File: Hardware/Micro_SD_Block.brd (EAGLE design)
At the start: 30.5 x 44.5 mm, 16 parts, among them U1 USD-SOCKETNEW, U2 EDISON_CONNECTOR_FULLMOUNTING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, U3 EDISON_CONNECTOR_FULLHEADER

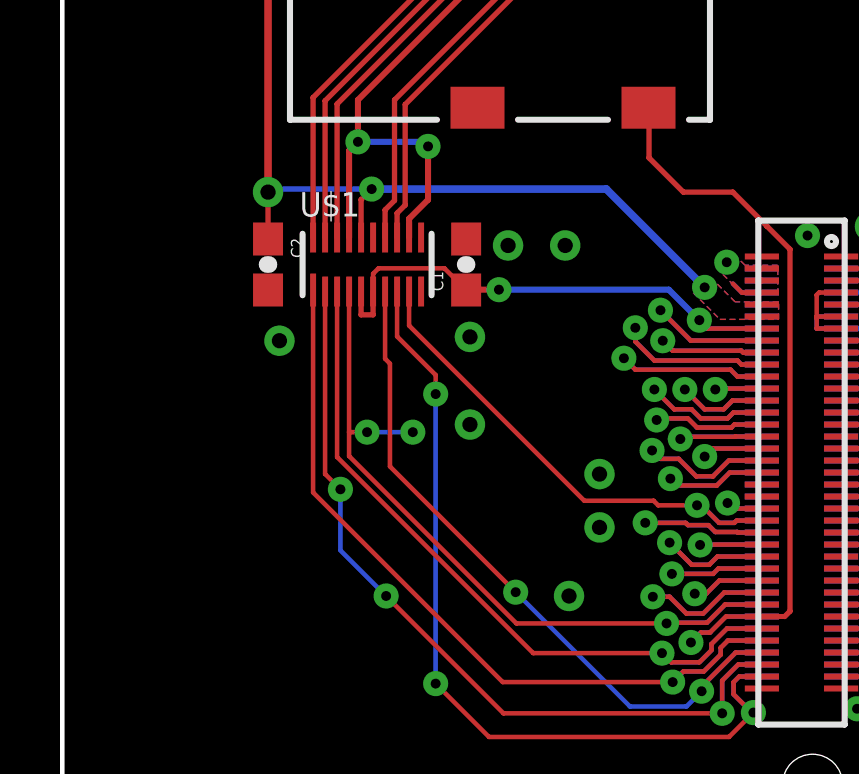
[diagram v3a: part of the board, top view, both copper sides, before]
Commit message: Ready for reds Struck one weird leftover via Renamed TXB0108 chip refdes To-do: fix the TXB0108 symbol to remove P$ from pin names. Do in library and update to design!
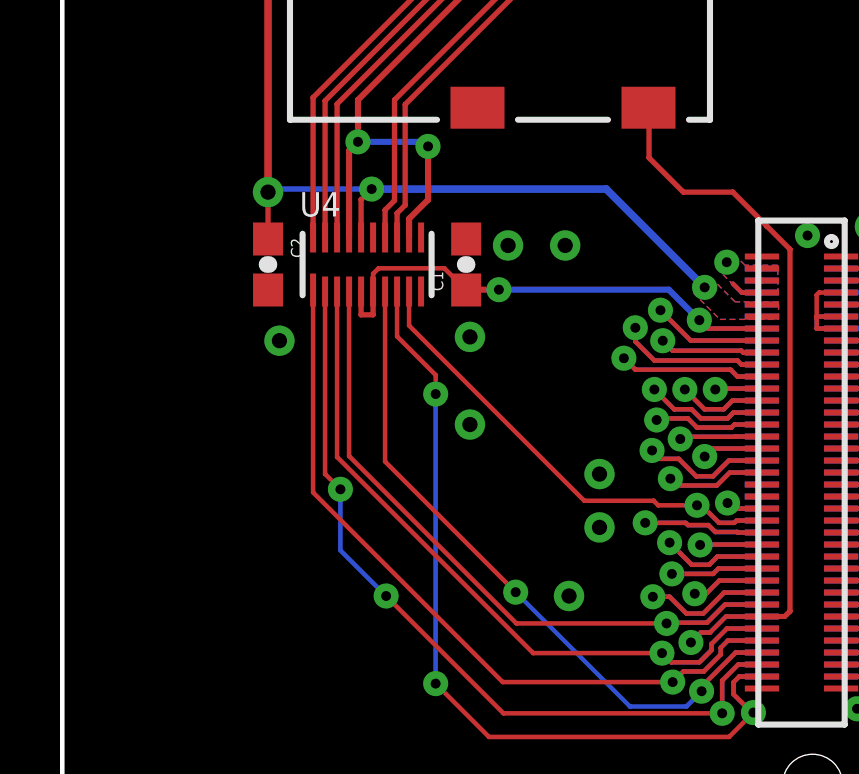
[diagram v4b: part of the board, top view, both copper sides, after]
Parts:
- renumbered U$1 to U4
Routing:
- net GP78_SD_0_CLK: track 27.4 -> 25.3 mm, vias 3 -> 1
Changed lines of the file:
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@@
 <setting verticaltext="up"/>
 </settings>
-<grid distance="0.005" unitdist="inch" unit="inch" style="lines" multiple="1" display="yes" altdistance="0.005" altunitdist="inch" altunit="inch"/>
+<grid distance="0.05" unitdist="inch" unit="inch" style="lines" multiple="1" display="yes" altdistance="0.005" altunitdist="inch" altunit="inch"/>
 <layers>
 <layer number="1" name="Top" color="4" fill="1" visible="yes" active="yes"/>
@@
 <layer number="21" name="tPlace" color="16" fill="1" visible="yes" active="yes"/>
 <layer number="22" name="bPlace" color="14" fill="1" visible="yes" active="yes"/>
-<layer number="23" name="tOrigins" color="15" fill="1" visible="no" active="yes"/>
-<layer number="24" name="bOrigins" color="15" fill="1" visible="no" active="yes"/>
+<layer number="23" name="tOrigins" color="15" fill="1" visible="yes" active="yes"/>
+<layer number="24" name="bOrigins" color="15" fill="1" visible="yes" active="yes"/>
 <layer number="25" name="tNames" color="7" fill="1" visible="no" active="yes"/>
 <layer number="26" name="bNames" color="7" fill="1" visible="no" active="yes"/>
@@
 <layer number="43" name="vRestrict" color="2" fill="10" visible="no" active="yes"/>
 <layer number="44" name="Drills" color="7" fill="1" visible="no" active="yes"/>
-<layer number="45" name="Holes" color="7" fill="1" visible="no" active="yes"/>
+<layer number="45" name="Holes" color="7" fill="1" visible="yes" active="yes"/>
 <layer number="46" name="Milling" color="3" fill="1" visible="no" active="yes"/>
-<layer number="51" name="tDocu" color="6" fill="1" visible="no" active="yes"/>
+<layer number="51" name="tDocu" color="6" fill="1" visible="yes" active="yes"/>
 <layer number="3" name="Route3" color="4" fill="3" visible="no" active="no"/>
 <layer number="4" name="Route4" color="1" fill="4" visible="no" active="no"/>
@@
 <layer number="251" name="SMDround" color="12" fill="11" visible="no" active="no"/>
 <layer number="254" name="cooling" color="7" fill="1" visible="no" active="no"/>
-<layer number="255" name="routoute" color="7" fill="1" visible="no" active="yes"/>
+<layer number="255" name="routoute" color="7" fill="1" visible="no" active="no"/>
 </layers>
 <board>
@@
 <element name="FID3" library="SparkFun-Aesthetics" package="FIDUCIAL-1X2" value="FIDUCIAL1X2" x="1.27" y="5.08" rot="MR0"/>
 <element name="FID4" library="SparkFun-Aesthetics" package="FIDUCIAL-1X2" value="FIDUCIAL1X2" x="25.4" y="43.18" rot="MR0"/>
-<element name="U$1" library="Testing" package="UFDFN-20" value="TXB0108" x="10.16" y="23.114"/>
+<element name="U4" library="Testing" package="UFDFN-20" value="TXB0108" x="10.16" y="23.114"/>
 <element name="C1" library="SparkFun-Capacitors" package="0603-CAP" value="0.1uF" x="13.462" y="23.114" rot="R90">
 <attribute name="PROD_ID" value="CAP-00810" x="13.462" y="23.114" size="1.778" layer="27" rot="R90" display="off"/>
@@
 <contactref element="U1" pad="CD2"/>
 <contactref element="U1" pad="GND1"/>
-<contactref element="U$1" pad="P$15"/>
+<contactref element="U4" pad="P$15"/>
 <contactref element="U1" pad="6"/>
 <contactref element="C1" pad="2"/>
@@
 <contactref element="U3" pad="8"/>
 <contactref element="U3" pad="10"/>
-<contactref element="U$1" pad="P$16"/>
+<contactref element="U4" pad="P$16"/>
 <contactref element="U1" pad="4"/>
 <via x="10.3124" y="25.6286" extent="1-16" drill="0.3302"/>
@@
 <wire x1="19.7104" y1="15.24" x2="19.8628" y2="15.0876" width="0.1524" layer="1"/>
 <wire x1="19.8628" y1="15.0876" x2="21.1582" y2="15.0876" width="0.1524" layer="1"/>
-<contactref element="U$1" pad="P$9"/>
+<contactref element="U4" pad="P$9"/>
 <wire x1="11.56" y1="22.214" x2="11.56" y2="21.079" width="0.1524" layer="1"/>
 <wire x1="11.56" y1="21.079" x2="17.399" y2="15.24" width="0.1524" layer="1"/>
@@
 <contactref element="U2" pad="58"/>
 <contactref element="U3" pad="58"/>
-<contactref element="U$1" pad="P$4"/>
-<wire x1="9.56" y1="22.214" x2="9.56" y2="17.526" width="0.1524" layer="1"/>
-<wire x1="9.56" y1="17.526" x2="9.56" y2="16.729" width="0.1524" layer="1"/>
+<contactref element="U4" pad="P$4"/>
+<wire x1="9.56" y1="22.214" x2="9.56" y2="16.729" width="0.1524" layer="1"/>
 <wire x1="9.56" y1="16.729" x2="15.1384" y2="11.1506" width="0.1524" layer="1"/>
 <wire x1="15.1384" y1="11.1506" x2="20.1422" y2="11.1506" width="0.1524" layer="1"/>
-<via x="11.684" y="17.526" extent="1-16" drill="0.3302"/>
-<wire x1="11.684" y1="17.526" x2="10.16" y2="17.526" width="0.1524" layer="16"/>
-<via x="10.16" y="17.526" extent="1-16" drill="0.3302"/>
-<wire x1="10.16" y1="17.526" x2="9.56" y2="17.526" width="0.1524" layer="1"/>
 </signal>
 <signal name="GP77_SD_0_CD#">
@@
 <contactref element="U2" pad="62"/>
 <contactref element="U3" pad="62"/>
-<contactref element="U$1" pad="P$3"/>
+<contactref element="U4" pad="P$3"/>
 <wire x1="9.16" y1="22.214" x2="9.16" y2="16.6972" width="0.1524" layer="1"/>
 <wire x1="9.16" y1="16.6972" x2="15.6972" y2="10.16" width="0.1524" layer="1"/>
@@
 <contactref element="U2" pad="66"/>
 <contactref element="U3" pad="66"/>
-<contactref element="U$1" pad="P$7"/>
+<contactref element="U4" pad="P$7"/>
 <wire x1="20.8026" y1="8.382" x2="21.3106" y2="8.89" width="0.1524" layer="16"/>
 <via x="15.113" y="12.192" extent="1-16" drill="0.3302"/>
-<wire x1="10.922" y1="16.383" x2="15.113" y2="12.192" width="0.1524" layer="1"/>
+<wire x1="10.76" y1="16.545" x2="15.113" y2="12.192" width="0.1524" layer="1"/>
 <wire x1="15.113" y1="12.192" x2="18.923" y2="8.382" width="0.1524" layer="16"/>
 <wire x1="18.923" y1="8.382" x2="20.8026" y2="8.382" width="0.1524" layer="16"/>
-<wire x1="10.76" y1="22.214" x2="10.76" y2="19.974" width="0.1524" layer="1"/>
-<wire x1="10.76" y1="19.974" x2="10.922" y2="19.812" width="0.1524" layer="1"/>
-<wire x1="10.922" y1="19.812" x2="10.922" y2="16.383" width="0.1524" layer="1"/>
+<wire x1="10.76" y1="22.214" x2="10.76" y2="16.545" width="0.1524" layer="1"/>
 </signal>
 <signal name="GP81_SD_0_DAT1">
@@
 <contactref element="U2" pad="70"/>
 <contactref element="U3" pad="70"/>
-<contactref element="U$1" pad="P$8"/>
+<contactref element="U4" pad="P$8"/>
 <wire x1="11.16" y1="22.214" x2="11.16" y2="20.717" width="0.1524" layer="1"/>
 <wire x1="11.16" y1="20.717" x2="12.446" y2="19.431" width="0.1524" layer="1"/>
@@
 <contactref element="U2" pad="64"/>
 <contactref element="U3" pad="64"/>
-<contactref element="U$1" pad="P$1"/>
+<contactref element="U4" pad="P$1"/>
 <wire x1="8.36" y1="22.264" x2="8.36" y2="15.516" width="0.1524" layer="1"/>
 <wire x1="8.36" y1="15.516" x2="14.6812" y2="9.1948" width="0.1524" layer="1"/>
@@
 <contactref element="U2" pad="68"/>
 <contactref element="U3" pad="68"/>
-<contactref element="U$1" pad="P$2"/>
+<contactref element="U4" pad="P$2"/>
 <wire x1="8.76" y1="22.214" x2="8.76" y2="16.132" width="0.1524" layer="1"/>
 <wire x1="8.76" y1="16.132" x2="9.271" y2="15.621" width="0.1524" layer="1"/>
@@
 <contactref element="U2" pad="12"/>
 <contactref element="U3" pad="12"/>
-<contactref element="U$1" pad="P$5"/>
+<contactref element="U4" pad="P$5"/>
 <contactref element="C1" pad="1"/>
-<contactref element="U$1" pad="P$6"/>
+<contactref element="U4" pad="P$6"/>
 <wire x1="10.36" y1="22.214" x2="10.36" y2="22.806" width="0.1524" layer="1"/>
 <wire x1="10.36" y1="22.806" x2="10.541" y2="22.987" width="0.1524" layer="1"/>
@@
 </signal>
 <signal name="N$1">
-<contactref element="U$1" pad="P$20"/>
+<contactref element="U4" pad="P$20"/>
 <contactref element="U1" pad="1"/>
 <wire x1="8.36" y1="24.014" x2="8.36" y2="28.68" width="0.1778" layer="1"/>
@@
 <signal name="N$2">
 <contactref element="U1" pad="2"/>
-<contactref element="U$1" pad="P$19"/>
+<contactref element="U4" pad="P$19"/>
 <wire x1="8.76" y1="24.014" x2="8.76" y2="28.572" width="0.1778" layer="1"/>
 <wire x1="8.76" y1="28.572" x2="13.75" y2="33.562" width="0.1778" layer="1"/>
@@
 </signal>
 <signal name="N$3">
-<contactref element="U$1" pad="P$18"/>
+<contactref element="U4" pad="P$18"/>
 <contactref element="U1" pad="3"/>
 <wire x1="9.16" y1="24.014" x2="9.16" y2="28.464" width="0.1778" layer="1"/>
@@
 </signal>
 <signal name="SCK">
-<contactref element="U$1" pad="P$17"/>
+<contactref element="U4" pad="P$17"/>
 <contactref element="U1" pad="5"/>
 <wire x1="17.05" y1="35.7952" x2="17.05" y2="38.64" width="0.1778" layer="1"/>
-<contactref element="U$1" pad="P$12"/>
+<contactref element="U4" pad="P$12"/>
 <via x="9.8552" y="27.2034" extent="1-16" drill="0.3302"/>
 <wire x1="9.56" y1="24.014" x2="9.56" y2="26.9082" width="0.2032" layer="1"/>
@@
 </signal>
 <signal name="N$5">
-<contactref element="U$1" pad="P$14"/>
+<contactref element="U4" pad="P$14"/>
 <contactref element="U1" pad="7"/>
 <wire x1="19.25" y1="36.776" x2="19.25" y2="38.64" width="0.1778" layer="1"/>
@@
 </signal>
 <signal name="N$6">
-<contactref element="U$1" pad="P$13"/>
+<contactref element="U4" pad="P$13"/>
 <contactref element="U1" pad="8"/>
 <wire x1="20.35" y1="37.368" x2="20.35" y2="38.64" width="0.1778" layer="1"/>

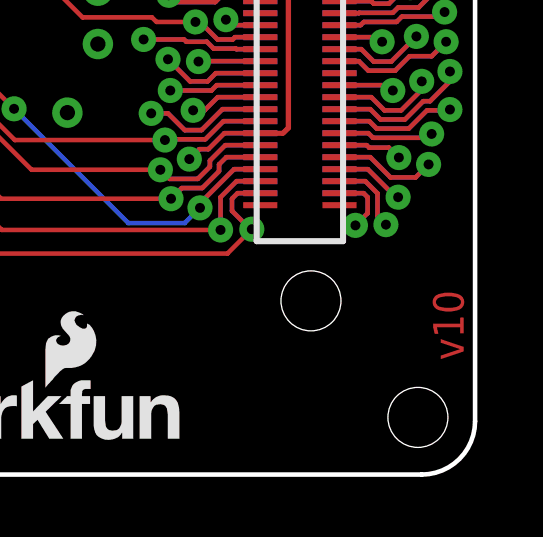
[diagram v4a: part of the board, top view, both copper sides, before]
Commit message: fixed CD grounding issue, CD1 and CD2 are connected internally.
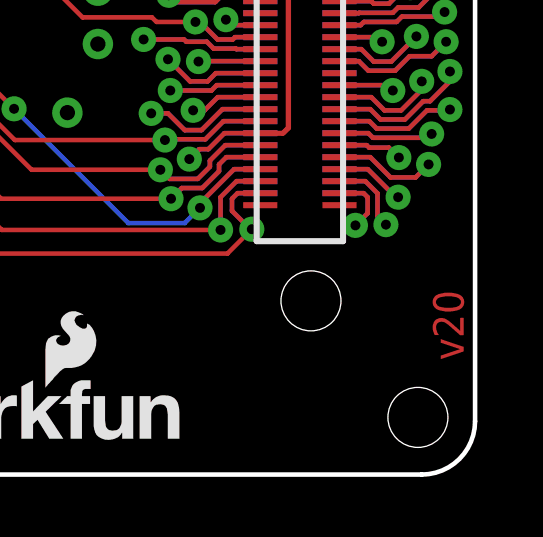
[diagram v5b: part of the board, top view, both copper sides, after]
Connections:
- net GND: no longer U1.CD2
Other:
- board text added: "v20"
- board text removed: "v10"
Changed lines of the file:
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@@
 <?xml version="1.0" encoding="utf-8"?>
 <!DOCTYPE eagle SYSTEM "eagle.dtd">
-<eagle version="6.6.0">
+<eagle version="6.5.0">
 <drawing>
 <settings>
@@
 <rectangle x1="22.098" y1="26.162" x2="30.48" y2="44.45" layer="41" rot="R180"/>
 <text x="29.21" y="6.35" size="1.016" layer="22" font="vector" ratio="15" rot="SMR270" align="center">4xM2.0</text>
-<text x="30.099" y="3.81" size="1.016" layer="1" font="vector" ratio="15" rot="R90">v10</text>
+<text x="30.099" y="3.81" size="1.016" layer="1" font="vector" ratio="15" rot="R90">v20</text>
 <text x="33.02" y="-2.54" size="1.778" layer="51">Note: Units are in Inches</text>
 <text x="29.972" y="41.148" size="1.27" layer="22" font="vector" ratio="15" rot="SMR270">Micro SD Block</text>
@@
 <contactref element="U3" pad="13"/>
 <contactref element="U1" pad="GND3"/>
-<contactref element="U1" pad="CD2"/>
 <contactref element="U1" pad="GND1"/>
 <contactref element="U4" pad="P$15"/>
